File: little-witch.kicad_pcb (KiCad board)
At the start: 4 copper layers, 65 x 30 mm, 56 parts, among them J1 GCT-USB4105, J2 TMJG0803HENL, J3 Conn_ARM_SWD_TagConnect_TC203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, J4 GCT-USB4105, J5 Conn_02x20_Odd_Even, J6 BOOT0_SEL, SW1 SW_Push, U1 CH32V307RCT6, U2 MXL86110C-AQB-R, Y1 SIT8008BI-73-33N-25.000000

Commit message: Routing tweaks
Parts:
- R8, R9: moved to B.Cu
- moved R8 60.3 mm to (160.4, 117.9), turned to -90 degrees
- moved R9 57.8 mm to (160.4, 112.1)
- moved J3 46.7 mm to (168.8, 132.1)
- moved R10 45.9 mm to (173.3, 106.0)
- moved R3 1.10 mm to (150.3, 125.5)
- moved R4 0.59 mm to (156.1, 125.5)
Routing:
- net GND: track 42.2 -> 52.7 mm
- net Net-(J4-CC1): track 0.00 -> 3.30 mm, vias 0 -> 1
- net Net-(J1-CC1): track 0.00 -> 3.29 mm, vias 0 -> 1
- net Net-(J1-CC2): track 0.00 -> 3.09 mm, vias 0 -> 1
- net Net-(J4-CC2): track 0.00 -> 3.08 mm, vias 0 -> 1
- net /PA6: track 39.3 -> 41.5 mm
- net /PB1: track 30.2 -> 31.2 mm
- net /PA5: track 36.2 -> 37.1 mm

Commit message: Routing tweaks
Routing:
- net VDD_ETH: track 29.8 -> 32.5 mm
- net /PA6: track 41.5 -> 40.9 mm
- net /PA4: track 31.9 -> 31.4 mm

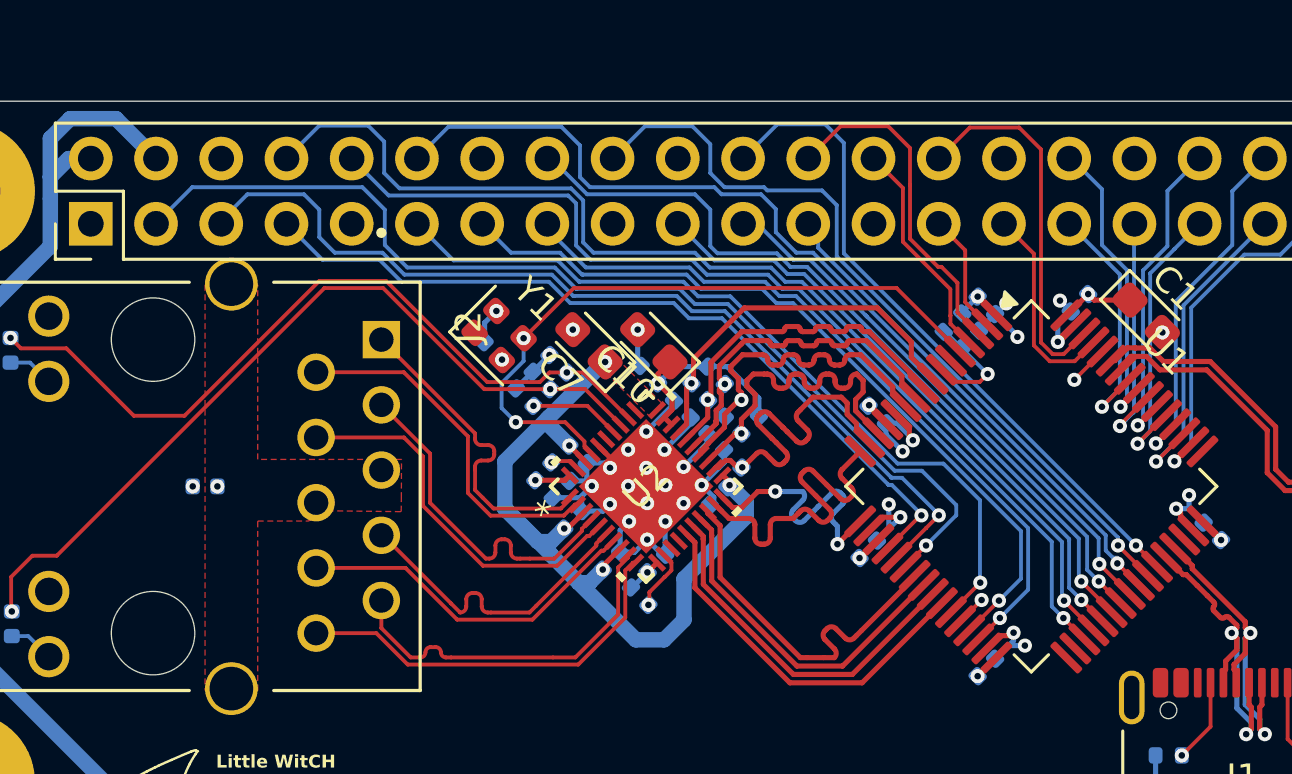
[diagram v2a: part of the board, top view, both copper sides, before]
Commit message: Start of better GPIO routing
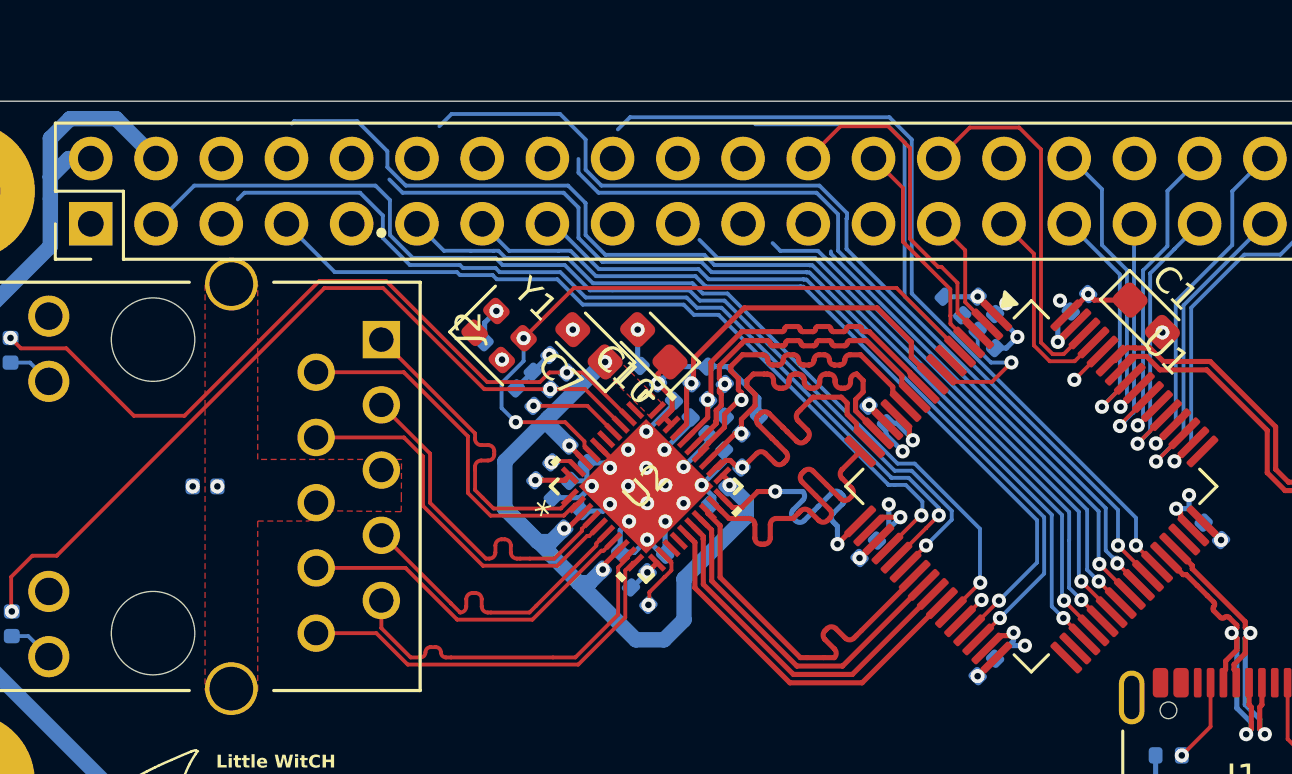
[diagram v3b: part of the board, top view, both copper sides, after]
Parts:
- moved R1 0.65 mm to (141.9, 108.0), turned to -45 degrees
- moved C8 0.62 mm to (143.2, 109.3), turned to 135 degrees
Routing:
- net /PA8: track 19.5 -> 37.7 mm
- net /PC7: track 31.1 -> 20.7 mm
- net /PC9: track 37.6 -> 30.8 mm
- net /PA10: track 26.3 -> 32.6 mm
- net /PA9: track 30.6 -> 26.9 mm
- net /PC8: track 21.7 -> 18.4 mm
- net NRST: track 4.49 -> 6.32 mm
- net /PB14: track 38.7 -> 37.3 mm
- net /PB10: track 30.6 -> 31.8 mm
- net /PA5: track 36.7 -> 35.6 mm
- net /PB11: track 28.9 -> 29.9 mm
- net /PB1: track 31.2 -> 30.6 mm
- net /PB15: track 43.1 -> 42.5 mm

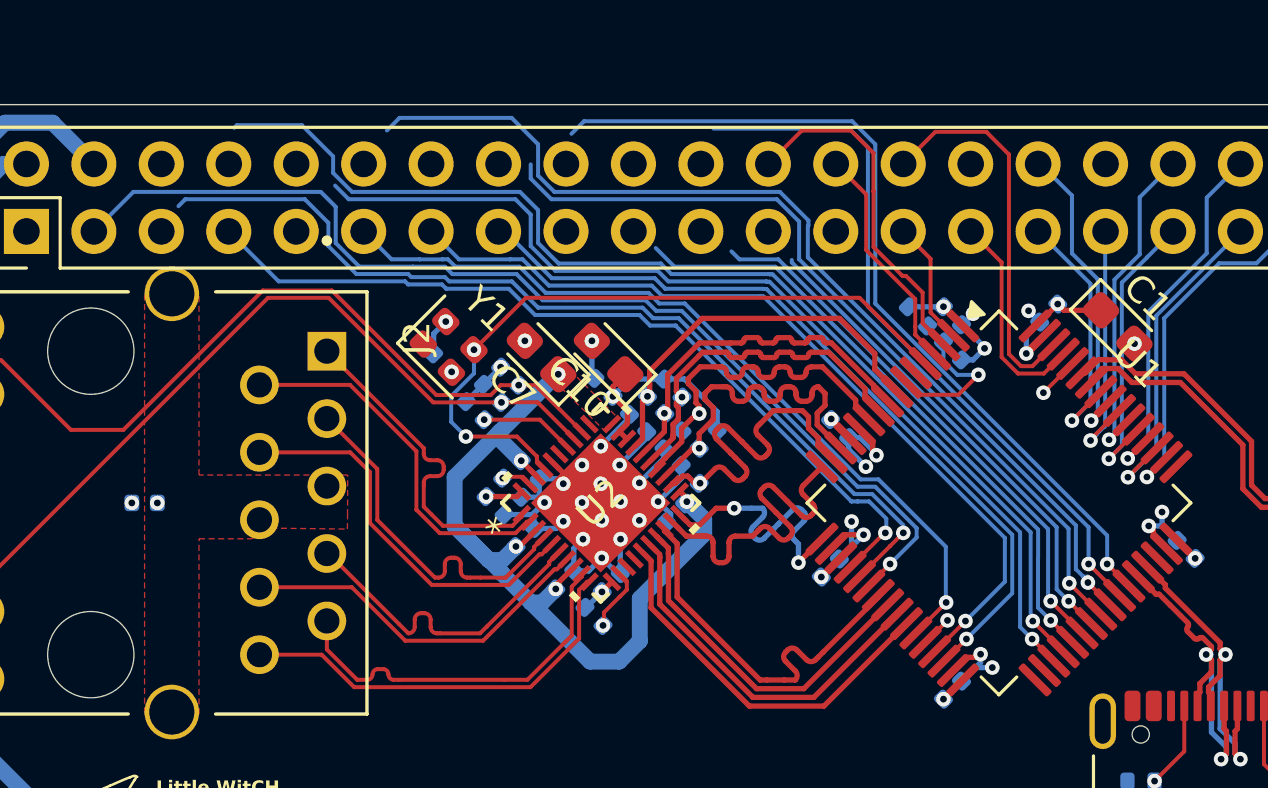
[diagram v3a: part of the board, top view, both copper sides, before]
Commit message: Better GPIO routing
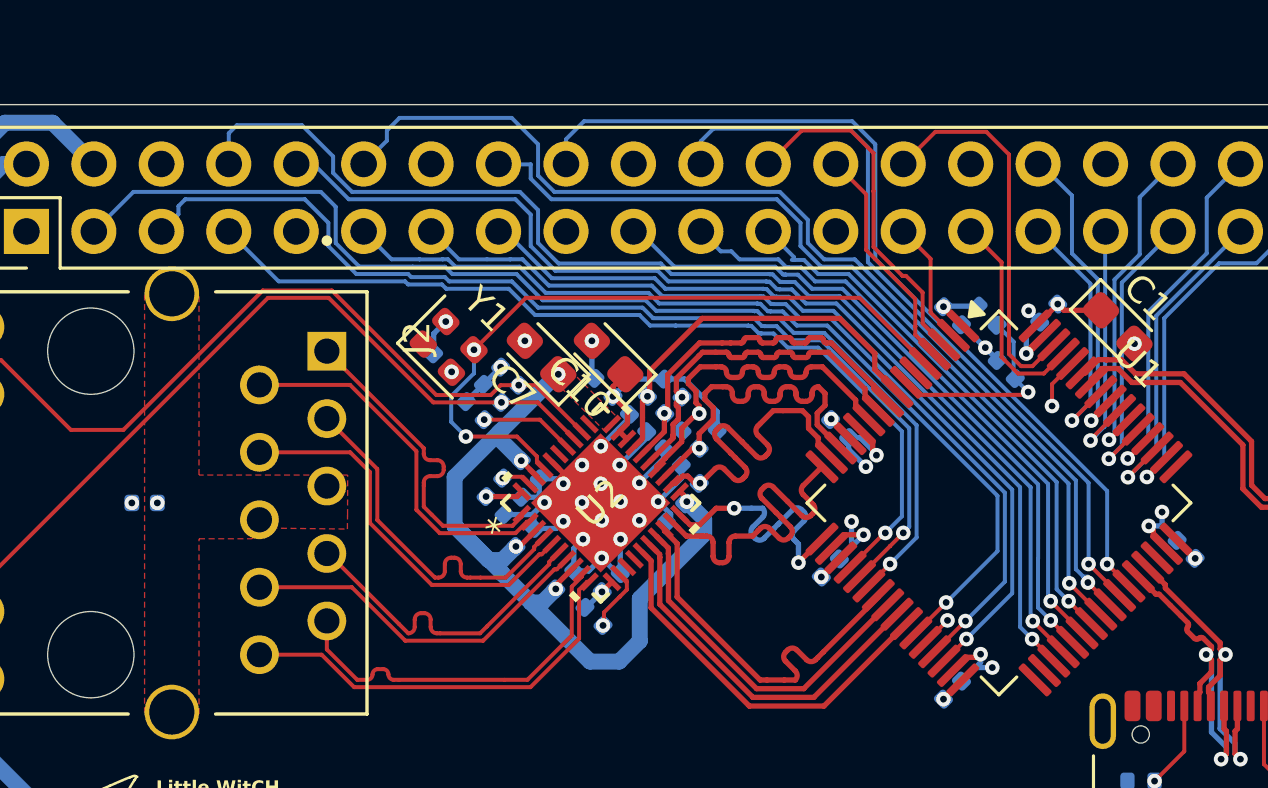
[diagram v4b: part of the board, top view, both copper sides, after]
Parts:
- moved R1 2.63 mm to (144.6, 108.0)
- moved C8 2.14 mm to (145.3, 110.0), turned to -45 degrees
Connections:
- J5 pad 12: /PC9 -> /PA8
- J5 pad 16: /PC7 -> /PC9
- J5 pad 18: /PA9 -> /PA10
- J5 pad 21: /PC8 -> /PC7
- J5 pad 22: /PA10 -> /PA9
- J5 pad 23: /PA8 -> /PC8
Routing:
- net /PB1: track 30.6 -> 34.4 mm
- net /PA5: track 35.6 -> 39.3 mm
- net /PB14: track 37.3 -> 40.1 mm
- net /PA4: track 31.7 -> 34.4 mm
- net /PC7: track 20.7 -> 23.2 mm
- net /PB15: track 42.5 -> 44.9 mm
- net /PC8: track 18.4 -> 20.8 mm
- net /PA8: track 37.7 -> 39.9 mm
- net /PA6: track 40.6 -> 42.8 mm
- net /PC6: track 23.6 -> 25.7 mm
- net /PC9: track 30.8 -> 32.7 mm
- net /PA9: track 26.9 -> 28.4 mm
- net NRST: track 6.32 -> 7.82 mm
- net /PA10: track 32.6 -> 33.8 mm
- net /PB11: track 29.9 -> 30.9 mm
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
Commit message: Power regulation
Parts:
- removed R1: 10k, Resistor_SMD:R_0402_1005Metric
- added C12: 4.7u, Capacitor_SMD:C_0805_2012Metric, F.Cu at (134.0, 125.9)
- added C13: 22u, Capacitor_SMD:C_0805_2012Metric, F.Cu at (129.0, 126.9)
- added L1: 1u, Inductor_SMD:L_1008_2520Metric, F.Cu at (130.0, 123.8)
- added R23: 450K ±1%, Resistor_SMD:R_0603_1608Metric, F.Cu at (131.5, 127.8)
- added R24: 100K ±1%, Resistor_SMD:R_0603_1608Metric, F.Cu at (134.5, 128.3)
- added U3: TPS62A0568PDRLR, Package_TO_SOT_SMD:SOT-563, F.Cu at (131.8, 126.2)
- moved R3 2.23 mm to (151.5, 127.4)
- moved C8 2.15 mm to (144.6, 108.0)
- moved R4 2.02 mm to (155.5, 127.4)
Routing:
- net USB1_VBUS: track 36.7 -> 92.1 mm, vias 0 -> 5
- net ETH_MDIO: track 0.00 -> 21.9 mm, vias 0 -> 2
- net ETH_MDC: track 0.00 -> 20.0 mm, vias 0 -> 2
- net Net-(U3-FB): track 0.00 -> 2.77 mm
- net Net-(J1-CC2): track 3.09 -> 5.07 mm
- net Net-(J1-CC1): track 3.29 -> 5.06 mm
- net USB1_DN: track 13.2 -> 11.5 mm
- net USB1_DP: track 13.2 -> 11.6 mm
- net +3V3: track 24.4 -> 25.8 mm, vias 11 -> 14
- net /TD4-: track 15.7 -> 16.5 mm
- net /TD4+: track 14.4 -> 15.2 mm
- net GND: track 51.9 -> 51.1 mm, vias 32 -> 40
- net /PA10: track 33.8 -> 33.2 mm
- net /PA9: track 28.4 -> 27.9 mm
- added copper zone on F.Cu, net +3V3
- added copper zone on F.Cu, net GND
- added copper zone on F.Cu, net Net-(U3-SW)
- added copper zone on F.Cu, net USB1_VBUS
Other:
- outline, holes or cut-outs redrawn
